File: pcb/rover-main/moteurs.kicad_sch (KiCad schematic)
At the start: 0 parts

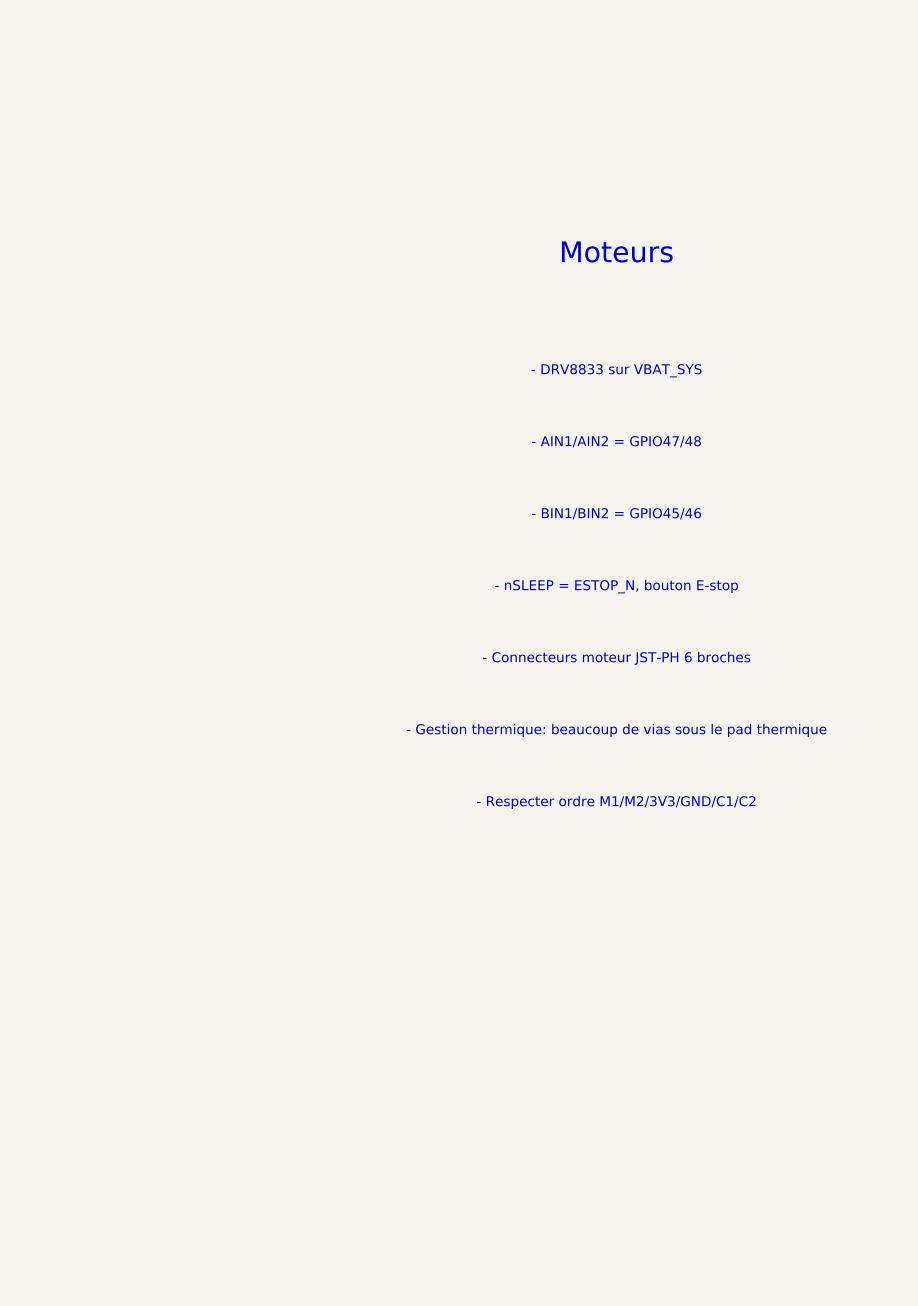
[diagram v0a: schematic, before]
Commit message: Add a more concrete KiCad schematic draft with key blocks and real net names for the Rover PCB design.
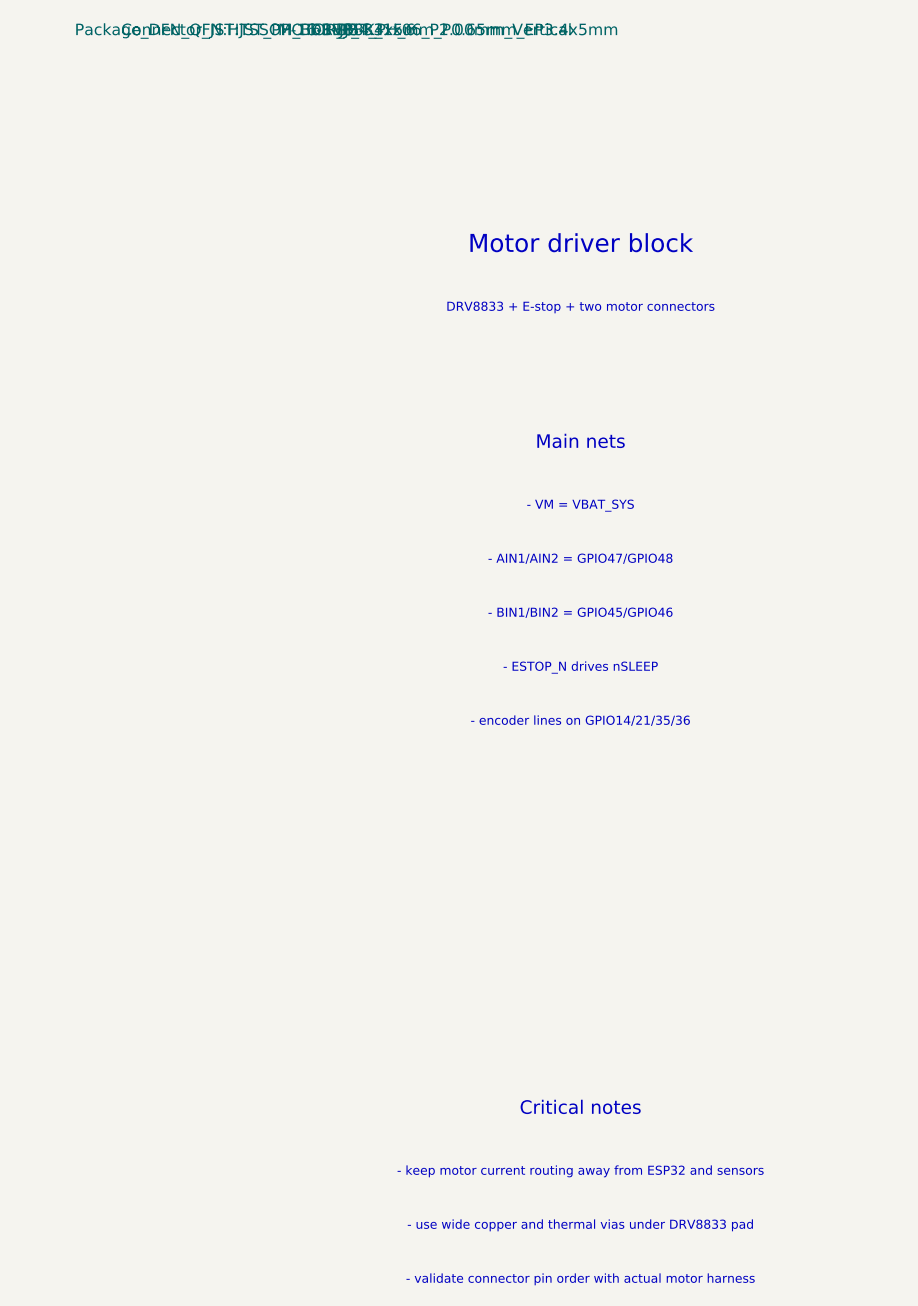
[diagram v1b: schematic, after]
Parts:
- added J3: MOTOR_JST_PH_6, Connector_JST:JST_PH_B6B-PH-K_1x06_P2.00mm_Vertical, symbol Connector_Generic:Conn_01x06
- added U2: DRV8833, Package_DFN_QFN:HTSSOP-16-1EP_4.4x5mm_P0.65mm_EP3.4x5mm, symbol Driver_Motor:DRV8833
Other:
- note added: "- AIN1/AIN2 = GPIO47/GPIO48"
- note added: "- BIN1/BIN2 = GPIO45/GPIO46"
- note added: "- ESTOP_N drives nSLEEP"
- note added: "- VM = VBAT_SYS"
- note added: "- encoder lines on GPIO14/21/35/36"
- note added: "- keep motor current routing away from ESP32 and sensors"
- note added: "- use wide copper and thermal vias under DRV8833 pad"
- note added: "- validate connector pin order with actual motor harness"
- note added: "Critical notes"
- note added: "DRV8833 + E-stop + two motor connectors"
- note added: "Main nets"
- note added: "Motor driver block"
- note removed: "- AIN1/AIN2 = GPIO47/48"
- note removed: "- BIN1/BIN2 = GPIO45/46"
- note removed: "- Connecteurs moteur JST-PH 6 broches"
- note removed: "- DRV8833 sur VBAT_SYS"
- note removed: "- Gestion thermique: beaucoup de vias sous le pad thermique"
- note removed: "- Respecter ordre M1/M2/3V3/GND/C1/C2"
- note removed: "- nSLEEP = ESTOP_N, bouton E-stop"
- note removed: "Moteurs"
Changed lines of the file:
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@@
 (kicad_sch
-  (version 20250114)
-  (generator "KiCad")
+  (version 20211014)
+  (generator "eeschema")
   (paper "A4")
   (title_block
     (title "Rover PCB - moteurs")
     (date "2026-10-13")
-    (rev "0.1")
+    (rev "0.2")
     (company "Rover Project")
-    (comment 1 "Draft only - validate motor connector order")
+    (comment 1 "Draft schematic - verify motor driver and encoder pin order")
   )
-  (text "Moteurs" (at 30 25 0)
-    (effects (font (size 2.3 2.3) (thickness 0.3)))
+  (text "Motor driver block" (at 26 24 0)
+    (effects (font (size 2.0 2.0) (thickness 0.2)))
   )
-  (text "- DRV8833 sur VBAT_SYS" (at 30 38 0)
-    (effects (font (size 1.1 1.1)))
+  (text "DRV8833 + E-stop + two motor connectors" (at 26 31 0)
+    (effects (font (size 1.0 1.0)))
   )
-  (text "- AIN1/AIN2 = GPIO47/48" (at 30 46 0)
-    (effects (font (size 1.1 1.1)))
+  (text "Main nets" (at 26 46 0)
+    (effects (font (size 1.5 1.5) (thickness 0.2)))
   )
-  (text "- BIN1/BIN2 = GPIO45/46" (at 30 54 0)
-    (effects (font (size 1.1 1.1)))
+  (text "- VM = VBAT_SYS" (at 26 53 0)
+    (effects (font (size 1.0 1.0)))
   )
-  (text "- nSLEEP = ESTOP_N, bouton E-stop" (at 30 62 0)
-    (effects (font (size 1.1 1.1)))
+  (text "- AIN1/AIN2 = GPIO47/GPIO48" (at 26 59 0)
+    (effects (font (size 1.0 1.0)))
   )
-  (text "- Connecteurs moteur JST-PH 6 broches" (at 30 70 0)
-    (effects (font (size 1.1 1.1)))
+  (text "- BIN1/BIN2 = GPIO45/GPIO46" (at 26 65 0)
+    (effects (font (size 1.0 1.0)))
   )
-  (text "- Gestion thermique: beaucoup de vias sous le pad thermique" (at 30 78 0)
-    (effects (font (size 1.1 1.1)))
+  (text "- ESTOP_N drives nSLEEP" (at 26 71 0)
+    (effects (font (size 1.0 1.0)))
   )
-  (text "- Respecter ordre M1/M2/3V3/GND/C1/C2" (at 30 86 0)
-    (effects (font (size 1.1 1.1)))
+  (text "- encoder lines on GPIO14/21/35/36" (at 26 77 0)
+    (effects (font (size 1.0 1.0)))
+  )
+  (symbol
+    (lib_id "Driver_Motor:DRV8833")
+    (at 150 105 0)
+    (unit 1)
+    (in_bom yes)
+    (property "Reference" "U2")
+    (property "Value" "DRV8833")
+    (property "Footprint" "Package_DFN_QFN:HTSSOP-16-1EP_4.4x5mm_P0.65mm_EP3.4x5mm")
+  )
+  (symbol
+    (lib_id "Connector_Generic:Conn_01x06")
+    (at 250 105 0)
+    (unit 1)
+    (in_bom yes)
+    (property "Reference" "J3")
+    (property "Value" "MOTOR_JST_PH_6")
+    (property "Footprint" "Connector_JST:JST_PH_B6B-PH-K_1x06_P2.00mm_Vertical")
+  )
+  (text "Critical notes" (at 26 120 0)
+    (effects (font (size 1.5 1.5) (thickness 0.2)))
+  )
+  (text "- keep motor current routing away from ESP32 and sensors" (at 26 127 0)
+    (effects (font (size 1.0 1.0)))
+  )
+  (text "- use wide copper and thermal vias under DRV8833 pad" (at 26 133 0)
+    (effects (font (size 1.0 1.0)))
+  )
+  (text "- validate connector pin order with actual motor harness" (at 26 139 0)
+    (effects (font (size 1.0 1.0)))
   )
 )
